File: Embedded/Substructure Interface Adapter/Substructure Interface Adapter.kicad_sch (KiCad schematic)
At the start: 3 parts, among them J1 Substructure Power, J2 Pogo Pins, U1 Substructure

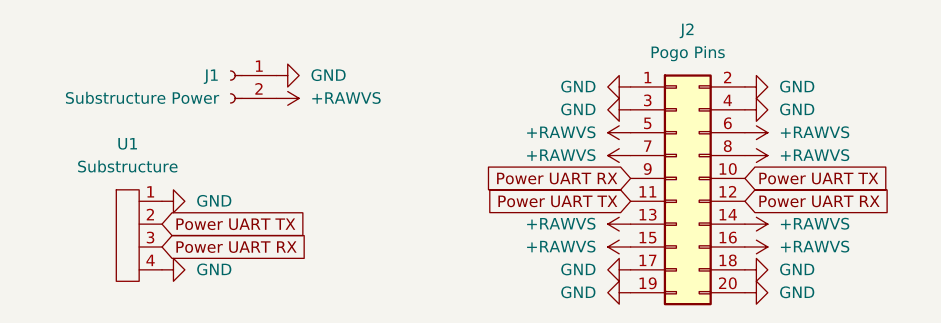
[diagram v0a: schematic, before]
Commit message: Modified UART Pins & Added Silkscreen Data
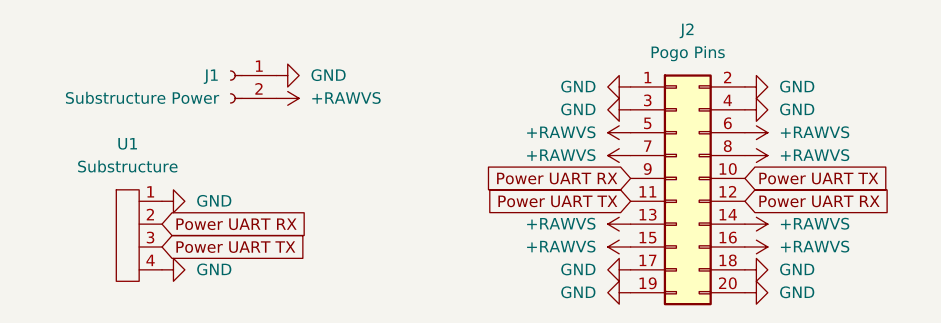
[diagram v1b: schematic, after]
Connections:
- net Power UART RX: now also U1.2; no longer U1.3
- net Power UART TX: now also U1.3; no longer U1.2
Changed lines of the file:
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@@
 	(global_label "Power UART TX"
 		(shape input)
-		(at 55.88 67.31 0)
+		(at 55.88 69.85 0)
 		(fields_autoplaced yes)
 		(effects
@@
 		)
 		(property "Intersheetrefs" "${INTERSHEET_REFS}"
-			(at 73.2585 67.31 0)
+			(at 73.2585 69.85 0)
 			(effects
 				(font
@@
 	(global_label "Power UART RX"
 		(shape input)
-		(at 55.88 69.85 0)
+		(at 55.88 67.31 0)
 		(fields_autoplaced yes)
 		(effects
@@
 		)
 		(property "Intersheetrefs" "${INTERSHEET_REFS}"
-			(at 73.5609 69.85 0)
+			(at 73.5609 67.31 0)
 			(effects
 				(font
